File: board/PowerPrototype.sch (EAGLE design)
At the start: 21 parts, among them IC1 7805T, Q1 IRF4905, T2 BT138-H

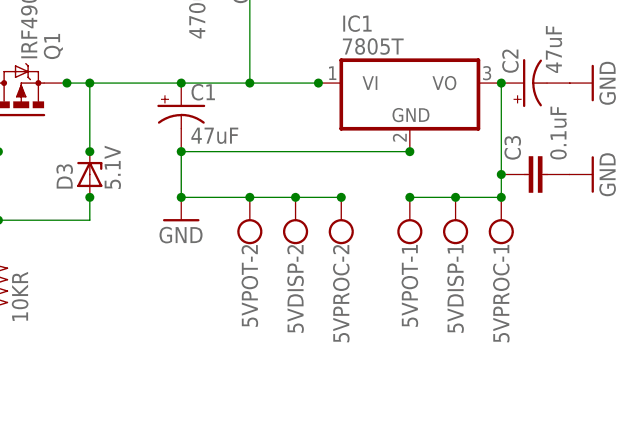
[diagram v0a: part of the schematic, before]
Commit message: Initial pass at a PCB and added clock code
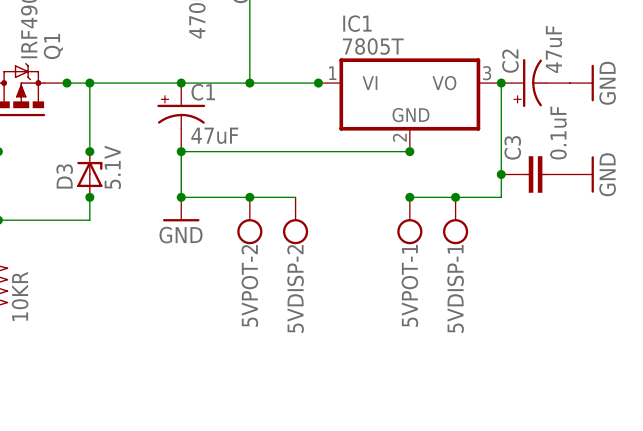
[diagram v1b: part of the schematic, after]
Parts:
- removed 5VPROC: (no value), con-wago-500:W237-102
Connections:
- net GND: no longer 5VPROC-2.KL
- net N$9: no longer 5VPROC-1.KL
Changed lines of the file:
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@@
 <part name="GND4" library="supply1" deviceset="GND" device=""/>
 <part name="GND5" library="supply1" deviceset="GND" device=""/>
-<part name="5VPROC" library="con-wago-500" deviceset="W237-102" device=""/>
 <part name="24VOUT" library="con-wago-500" deviceset="W237-102" device=""/>
 <part name="5VPOT" library="con-wago-500" deviceset="W237-102" device=""/>
@@
 <instance part="GND4" gate="1" x="-12.7" y="20.32"/>
 <instance part="GND5" gate="1" x="38.1" y="66.04" rot="R270"/>
-<instance part="5VPROC" gate="-1" x="76.2" y="35.56" rot="R90"/>
-<instance part="5VPROC" gate="-2" x="58.42" y="35.56" rot="R90"/>
 <instance part="24VOUT" gate="-1" x="40.64" y="83.82" rot="R270"/>
 <instance part="24VOUT" gate="-2" x="48.26" y="83.82" rot="R270"/>
@@
 <junction x="66.04" y="45.72"/>
 <junction x="40.64" y="45.72"/>
-<pinref part="5VPROC" gate="-2" pin="KL"/>
 <pinref part="5VDISP" gate="-2" pin="KL"/>
-<wire x1="58.42" y1="40.64" x2="53.34" y2="40.64" width="0.1524" layer="91"/>
 <pinref part="5VPOT" gate="-2" pin="KL"/>
 <wire x1="53.34" y1="40.64" x2="48.26" y2="40.64" width="0.1524" layer="91"/>
-<junction x="53.34" y="40.64"/>
 <wire x1="48.26" y1="40.64" x2="40.64" y2="40.64" width="0.1524" layer="91"/>
 <junction x="48.26" y="40.64"/>
 <junction x="40.64" y="40.64"/>
-<junction x="58.42" y="40.64"/>
 </segment>
 <segment>
@@
 <pinref part="5VDISP" gate="-1" pin="KL"/>
 <wire x1="66.04" y1="40.64" x2="71.12" y2="40.64" width="0.1524" layer="91"/>
-<pinref part="5VPROC" gate="-1" pin="KL"/>
 <wire x1="71.12" y1="40.64" x2="76.2" y2="40.64" width="0.1524" layer="91"/>
 <junction x="71.12" y="40.64"/>
 <pinref part="IC1" gate="A1" pin="VO"/>
 <wire x1="76.2" y1="40.64" x2="76.2" y2="43.18" width="0.1524" layer="91"/>
-<junction x="76.2" y="40.64"/>
 <junction x="66.04" y="40.64"/>
 <junction x="76.2" y="53.34"/>
